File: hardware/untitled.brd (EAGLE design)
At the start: 68.6 x 47.9 mm, 47 parts, among them IC2 LM1117IMPX-3.3, U4 microSD, Y1 CRYSTAL-GROUNDEDSMD-5X3.2

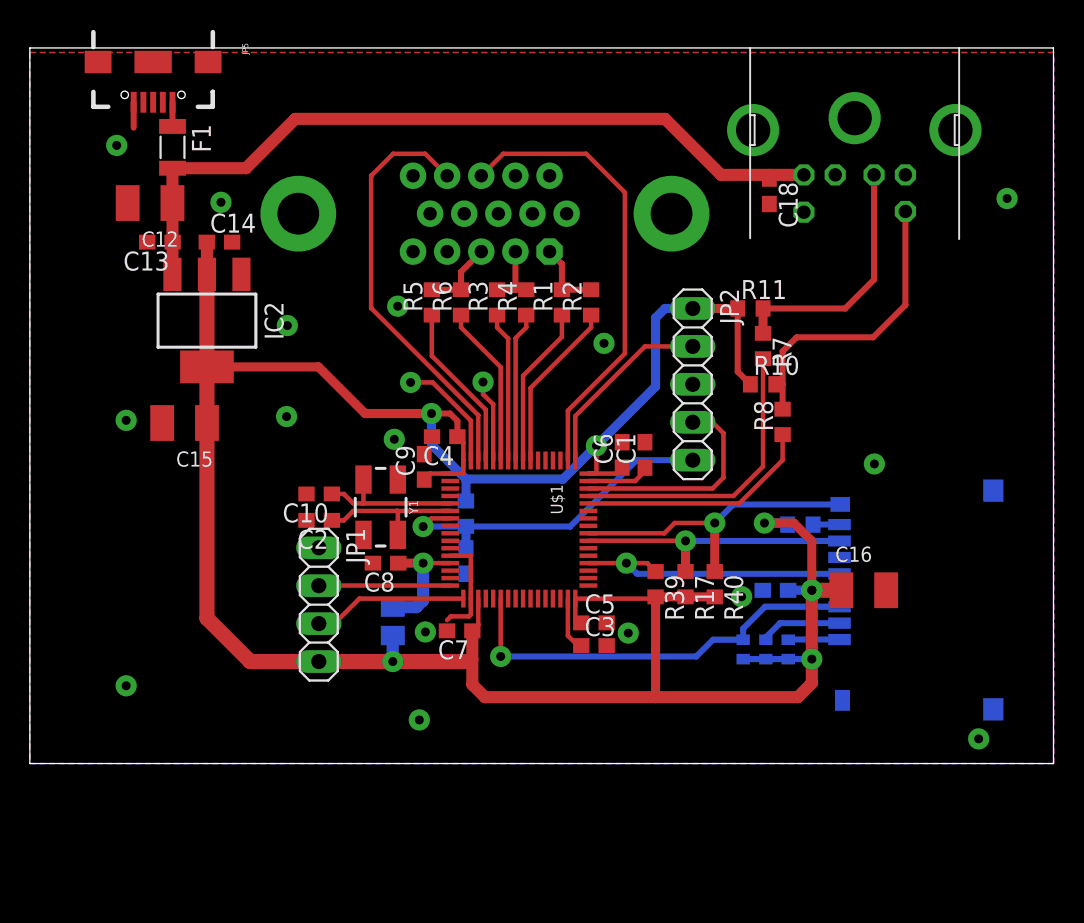
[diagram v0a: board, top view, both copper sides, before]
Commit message: Proper MCU footprint used
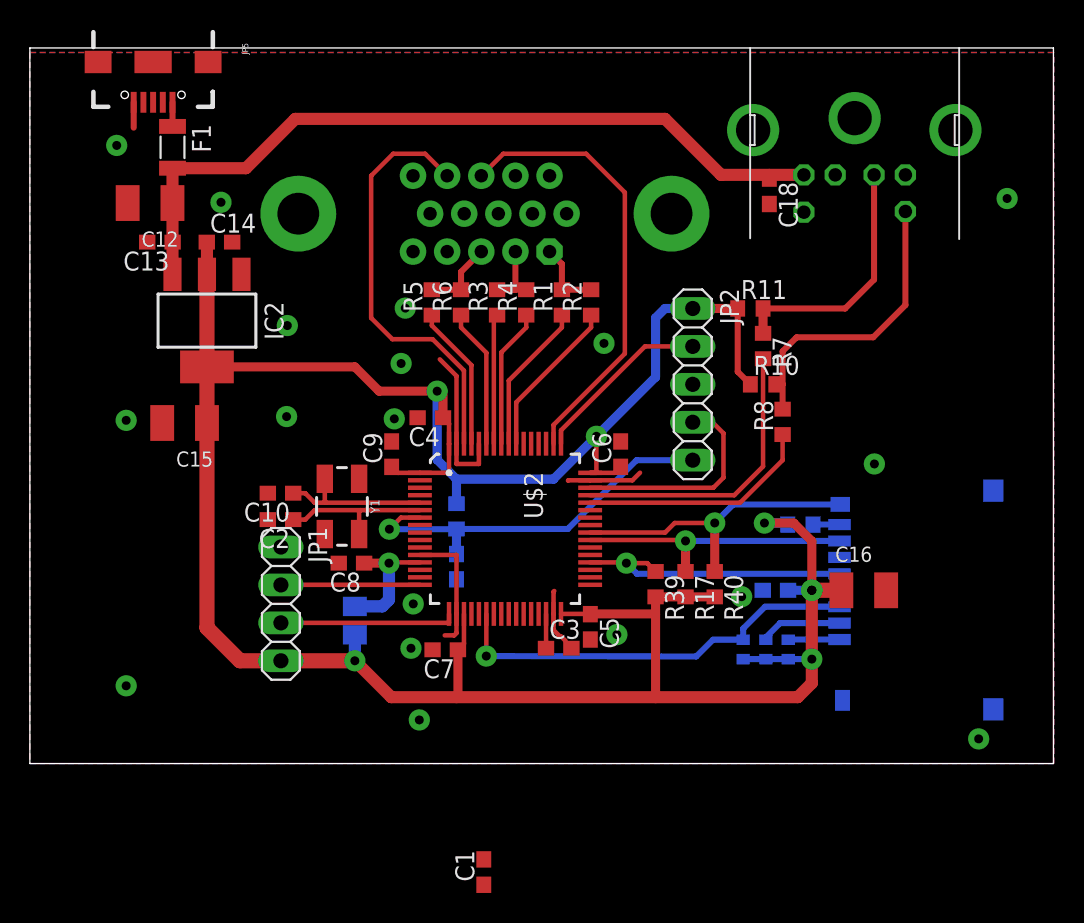
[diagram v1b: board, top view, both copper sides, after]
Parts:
- removed U$1: STM32F4R_64PIN_FOXCAR, stm32f4:LQFP64
- added U$2: STM32F411XC, stm32f411:LQFP64
- moved C1 30.0 mm to (30.4, -7.27)
- moved Y1 2.59 mm to (20.9, 17.2)
- moved C10 2.59 mm to (16.8, 18.1)
- moved C2 2.59 mm to (16.8, 16.3)
- moved JP1 2.54 mm to (16.8, 10.7)
- moved R9 2.54 mm to (21.8, 9.58)
- moved C3 2.37 mm to (35.4, 7.72)
- moved C9 2.34 mm to (24.2, 20.7)
- moved C8 2.29 mm to (21.5, 13.4)
- moved C4 1.60 mm to (26.8, 23.2)
- moved C7 1.60 mm to (27.8, 7.62)
- moved C17 0.74 mm to (28.6, 13.2)
- moved R12 0.66 mm to (28.6, 16.6)
- moved C5 0.36 mm to (37.5, 9.16), turned to 270 degrees
- moved C6 0.11 mm to (39.6, 20.7)
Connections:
- net 3V: now also U$2.1, U$2.19, U$2.32, U$2.48, U$2.64; no longer U$1.1, U$1.19, U$1.32, U$1.48, U$1.64
- net BLUE0: now also U$2.59; no longer U$1.59
- net BLUE1: now also U$2.61; no longer U$1.61
- net GND: now also U$2.12, U$2.18, U$2.31, U$2.47, U$2.60, U$2.63; no longer U$1.12, U$1.18, U$1.60, U$1.63
- net GREEN0: now also U$2.57; no longer U$1.57
- net GREEN1: now also U$2.58; no longer U$1.58
- net HSYNC: now also U$2.50; no longer U$1.50
- net N$6: now also U$2.13; no longer U$1.13
- net N$7: no longer U$1.47
- net N$8: now also U$2.30; no longer U$1.31
- net NRST: now also U$2.7; no longer U$1.7
- net OSC_IN: now also U$2.5; no longer U$1.5
- net OSC_OUT: now also U$2.6; no longer U$1.6
- net PS2_CLK: now also U$2.44; no longer U$1.44
- net PS2_DAT: now also U$2.45; no longer U$1.45
- net RED0: now also U$2.55; no longer U$1.55
- net RED1: now also U$2.56; no longer U$1.56
- net SDIO_CD: now also U$2.40; no longer U$1.40
- net SDIO_CLK: now also U$2.36; no longer U$1.36
- net SDIO_CMD: now also U$2.22; no longer U$1.22
- net SDIO_D0: now also U$2.39; no longer U$1.39
- net SWD_CLK: now also U$2.49; no longer U$1.49
- net SWD_IO: now also U$2.46; no longer U$1.46
- net UART2_RX: now also U$2.17; no longer U$1.17
- net UART2_TX: now also U$2.16; no longer U$1.16
- net VSYNC: now also U$2.62; no longer U$1.62
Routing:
- net GND: track 22.1 -> 29.4 mm
- net N$7: track 4.30 -> 0.00 mm
- net 3V: track 185.5 -> 188.9 mm
- net NRST: track 23.4 -> 26.3 mm
- net BLUE1: track 11.2 -> 9.71 mm
- net BLUE0: track 10.8 -> 9.32 mm
- net UART2_RX: track 10.4 -> 11.9 mm
- net N$8: track 3.66 -> 2.30 mm
- net GREEN1: track 10.0 -> 8.70 mm
- net N$6: track 8.20 -> 9.07 mm
- net RED0: track 11.4 -> 10.7 mm
- net SWD_CLK: track 12.8 -> 12.0 mm
- net RED1: track 10.8 -> 10.1 mm
- net HSYNC: track 30.8 -> 30.1 mm
- net GREEN0: track 10.0 -> 9.31 mm
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
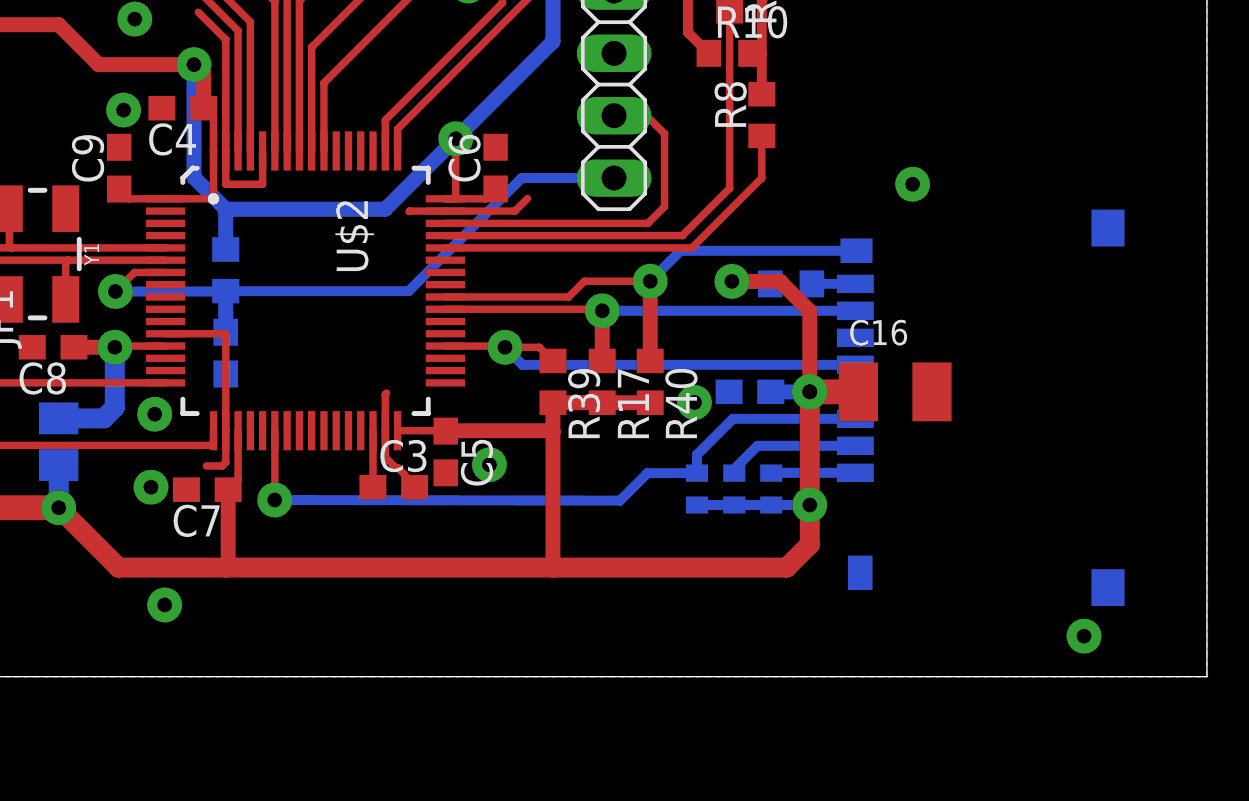
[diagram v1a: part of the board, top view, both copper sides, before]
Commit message: Capacitor removed
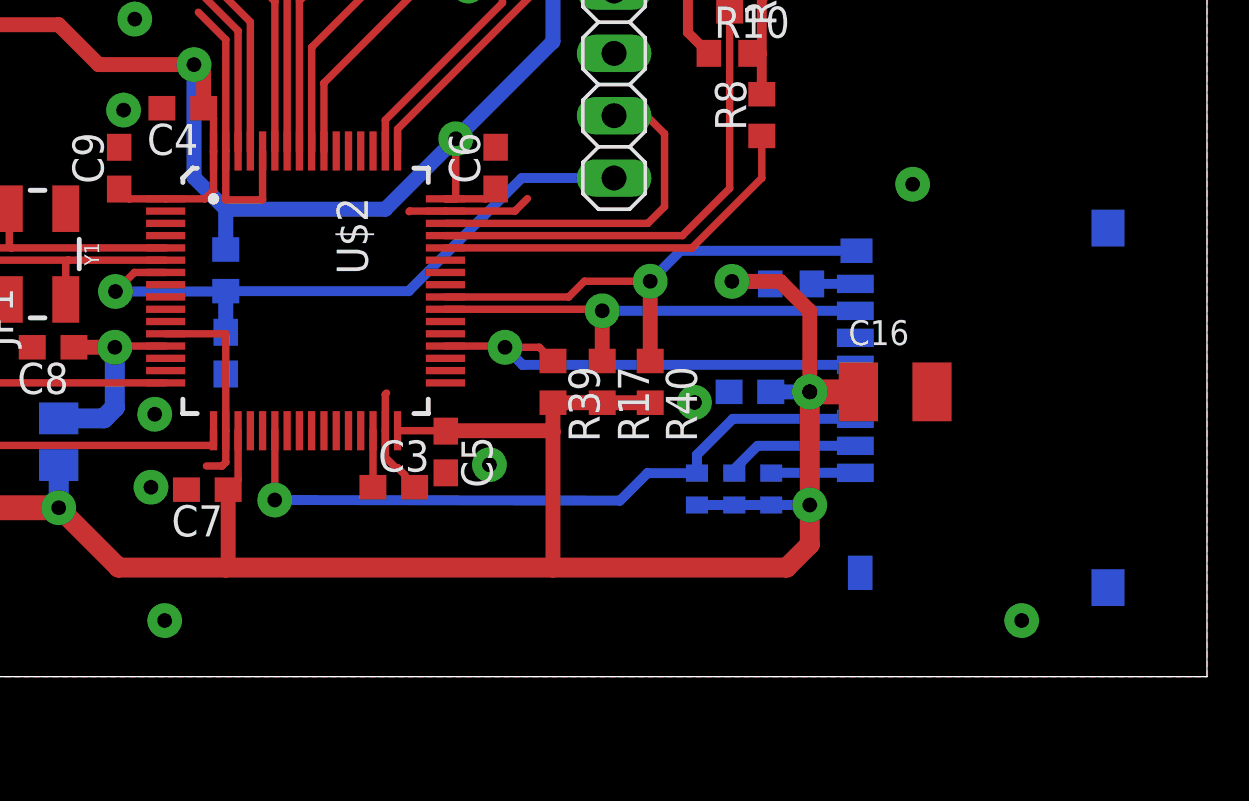
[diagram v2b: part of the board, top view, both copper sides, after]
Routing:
- net GND: track 29.4 -> 30.6 mm
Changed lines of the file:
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@@
 <via x="6.4516" y="5.207" extent="1-16" drill="0.6" diameter="1.4224" shape="octagon"/>
 <via x="65.4558" y="37.846" extent="1-16" drill="0.6" diameter="1.4224" shape="octagon"/>
-<via x="63.5508" y="1.651" extent="1-16" drill="0.6" diameter="1.4224" shape="octagon"/>
+<via x="61.0108" y="2.286" extent="1-16" drill="0.6" diameter="1.4224" shape="octagon"/>
 <via x="17.1958" y="23.241" extent="1-16" drill="0.6" diameter="1.4224" shape="octagon"/>
-<via x="26.0858" y="2.921" extent="1-16" drill="0.6" diameter="1.4224" shape="octagon"/>
+<via x="26.0858" y="2.286" extent="1-16" drill="0.6" diameter="1.4224" shape="octagon"/>
 <contactref element="C18" pad="2"/>
 <contactref element="U$2" pad="12"/>
@@
 <wire x1="28.5762" y1="21.4226" x2="28.5762" y2="25.9576" width="0.3048" layer="1"/>
 <wire x1="28.5762" y1="25.9576" x2="27.4574" y2="27.0764" width="0.3048" layer="1"/>
-<wire x1="28.5762" y1="21.4226" x2="28.5762" y2="20.066" width="0.3048" layer="1"/>
-<wire x1="28.5762" y1="20.066" x2="30.0762" y2="20.066" width="0.3048" layer="1"/>
-<wire x1="30.0762" y1="20.066" x2="30.0762" y2="21.4226" width="0.3048" layer="1"/>
+<wire x1="28.5762" y1="21.4226" x2="28.5762" y2="19.431" width="0.3048" layer="1"/>
+<wire x1="28.5762" y1="19.431" x2="30.0762" y2="19.431" width="0.3048" layer="1"/>
+<wire x1="30.0762" y1="19.431" x2="30.0762" y2="21.4226" width="0.3048" layer="1"/>
 <via x="24.8666" y="26.797" extent="1-16" drill="0.6" diameter="1.4224" shape="octagon"/>
 <wire x1="28.5762" y1="10.0226" x2="28.5762" y2="8.7388" width="0.3048" layer="1"/>
@@
 <wire x1="37.5262" y1="18.9726" x2="40.3594" y2="18.9726" width="0.3048" layer="1"/>
 <wire x1="40.3594" y1="18.9726" x2="40.8686" y2="19.4818" width="0.3048" layer="1"/>
-<wire x1="26.0858" y1="2.921" x2="30.4038" y2="-6.41948125" width="0" layer="19" extent="1-1"/>
+<wire x1="26.0858" y1="2.286" x2="30.4038" y2="-6.41948125" width="0" layer="19" extent="1-1"/>
 </signal>
 <signal name="PE1">
@@
 <wire x1="28.0762" y1="21.4226" x2="28.0762" y2="22.761" width="0.3048" layer="1"/>
 <wire x1="28.0762" y1="22.761" x2="27.6724" y2="23.1648" width="0.3048" layer="1"/>
-<wire x1="26.1262" y1="19.4726" x2="28.0762" y2="19.4726" width="0.3048" layer="1"/>
-<wire x1="28.0762" y1="19.4726" x2="28.0762" y2="21.4226" width="0.3048" layer="1"/>
 <wire x1="27.6724" y1="23.1648" x2="27.6724" y2="24.9428" width="0.6096" layer="1"/>
 <wire x1="27.2796" y1="24.9428" x2="23.3934" y2="24.9428" width="0.6096" layer="1"/>
@@
 <wire x1="37.9476" y1="21.9202" x2="37.9476" y2="19.4726" width="0.3048" layer="1"/>
 <wire x1="37.9476" y1="19.4726" x2="37.5262" y2="19.4726" width="0.3048" layer="1"/>
+<wire x1="26.1262" y1="19.4726" x2="27.7276" y2="19.4726" width="0.3048" layer="1"/>
+<wire x1="27.7276" y1="19.4726" x2="28.0762" y2="19.8212" width="0.3048" layer="1"/>
+<wire x1="28.0762" y1="21.4226" x2="28.0762" y2="19.8212" width="0.3048" layer="1"/>
 </signal>
 <signal name="5V">

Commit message: Minor adjustment
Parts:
- removed C1: (no value), rcl:C0603
- moved C12 1.65 mm to (8.05, 35.9)
- moved C15 1.65 mm to (10.4, 21.2)
- moved IC2 1.65 mm to (11.9, 28.0)
- moved C13 1.65 mm to (8.71, 33.3)
- moved C14 1.65 mm to (12.7, 33.3)
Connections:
- removed net N$7: C1.1
- net GND: no longer C1.2
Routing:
- net 3V: track 188.7 -> 186.4 mm
- net 5V: track 52.7 -> 54.3 mm
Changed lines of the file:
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@@
 <attribute name="OC_FARNELL" value="1596988" x="31.78" y="49.53" size="1.778" layer="27" rot="R270" display="off"/>
 </element>
-<element name="C12" library="rcl" package="SMC_B" value="" x="8.0518" y="37.5412" rot="R180"/>
-<element name="C13" library="rcl" package="C0603" value="" x="8.7122" y="34.925" rot="R180"/>
-<element name="C14" library="rcl" package="C0603" value="" x="12.7" y="34.925"/>
-<element name="C15" library="rcl" package="SMC_B" value="" x="10.3632" y="22.8092" rot="R180"/>
-<element name="IC2" library="lm1117" package="SOT223" value="LM1117IMPX-3.3" x="11.8618" y="29.6672" rot="R180"/>
+<element name="C12" library="rcl" package="SMC_B" value="" x="8.0518" y="35.8902" rot="R180"/>
+<element name="C13" library="rcl" package="C0603" value="" x="8.7122" y="33.274" rot="R180"/>
+<element name="C14" library="rcl" package="C0603" value="" x="12.7" y="33.274"/>
+<element name="C15" library="rcl" package="SMC_B" value="" x="10.3632" y="21.1582" rot="R180"/>
+<element name="IC2" library="lm1117" package="SOT223" value="LM1117IMPX-3.3" x="11.8618" y="28.0162" rot="R180"/>
 <element name="JP2" library="pinhead" package="1X05" value="" x="44.3992" y="25.4" rot="R270"/>
 <element name="JP1" library="pinhead" package="1X04" value="" x="16.8148" y="10.6934" rot="R270"/>
@@
 <element name="C10" library="rcl" package="C0603" value="22 pF" x="16.7894" y="18.1084" rot="R180"/>
 <element name="Y1" library="SparkFun-Clocks" package="CRYSTAL-SMD-5X3.2-4PAD" value="CRYSTAL-GROUNDEDSMD-5X3.2" x="20.9042" y="17.2212" rot="R270"/>
-<element name="C1" library="rcl" package="C0603" value="" x="30.4038" y="-7.26948125" rot="R90"/>
 <element name="C3" library="rcl" package="C0603" value="" x="35.42156875" y="7.7216"/>
 <element name="U4" library="SparkFun-Connectors" package="USD-SOCKET-PP" value="microSD" x="68.5292" y="11.5062" rot="MR270"/>
@@
 <contactref element="Y1" pad="4"/>
 <contactref element="Y1" pad="2"/>
-<contactref element="C1" pad="2"/>
 <contactref element="C3" pad="2"/>
 <contactref element="U4" pad="6"/>
@@
 <via x="25.146" y="30.5054" extent="1-16" drill="0.6" diameter="1.4224" shape="octagon"/>
 <contactref element="C9" pad="2"/>
-<via x="12.8016" y="37.592" extent="1-16" drill="0.6" diameter="1.4224" shape="octagon"/>
+<via x="12.8016" y="35.941" extent="1-16" drill="0.6" diameter="1.4224" shape="octagon"/>
 <via x="17.2466" y="29.337" extent="1-16" drill="0.6" diameter="1.4224" shape="octagon"/>
-<via x="6.4516" y="22.987" extent="1-16" drill="0.6" diameter="1.4224" shape="octagon"/>
+<via x="6.4516" y="21.336" extent="1-16" drill="0.6" diameter="1.4224" shape="octagon"/>
 <via x="5.8166" y="41.402" extent="1-16" drill="0.6" diameter="1.4224" shape="octagon"/>
 <contactref element="C11" pad="2"/>
@@
 <wire x1="37.5262" y1="18.9726" x2="40.3594" y2="18.9726" width="0.3048" layer="1"/>
 <wire x1="40.3594" y1="18.9726" x2="40.8686" y2="19.4818" width="0.3048" layer="1"/>
-<wire x1="26.0858" y1="2.286" x2="30.4038" y2="-6.41948125" width="0" layer="19" extent="1-1"/>
 </signal>
 <signal name="PE1">
@@
 <contactref element="IC2" pad="TAB"/>
 <contactref element="IC2" pad="2"/>
-<wire x1="11.8618" y1="32.7662" x2="11.8618" y2="34.9132" width="0.8128" layer="1"/>
-<wire x1="11.8618" y1="34.9132" x2="11.85" y2="34.925" width="0.6096" layer="1"/>
+<wire x1="11.8618" y1="31.1152" x2="11.8618" y2="33.2622" width="0.8128" layer="1"/>
+<wire x1="11.8618" y1="33.2622" x2="11.85" y2="33.274" width="0.6096" layer="1"/>
 <contactref element="JP2" pad="1"/>
 <contactref element="JP1" pad="4"/>
@@
 <via x="37.9476" y="21.9202" extent="1-16" drill="0.6" diameter="1.4224" shape="octagon"/>
 <contactref element="C9" pad="1"/>
-<wire x1="11.8618" y1="32.7662" x2="11.8618" y2="26.5682" width="1.016" layer="1"/>
-<wire x1="11.8632" y1="22.8092" x2="11.8632" y2="26.5668" width="1.016" layer="1"/>
-<wire x1="11.8632" y1="26.5668" x2="11.8618" y2="26.5682" width="1.016" layer="1"/>
-<wire x1="11.8618" y1="26.5682" x2="21.768" y2="26.5682" width="0.6096" layer="1"/>
-<wire x1="11.8632" y1="22.8092" x2="11.8632" y2="9.0918" width="1.016" layer="1"/>
+<wire x1="11.8618" y1="31.1152" x2="11.8618" y2="24.9172" width="1.016" layer="1"/>
+<wire x1="11.8632" y1="21.1582" x2="11.8632" y2="24.9158" width="1.016" layer="1"/>
+<wire x1="11.8632" y1="24.9158" x2="11.8618" y2="24.9172" width="1.016" layer="1"/>
+<wire x1="11.8632" y1="21.1582" x2="11.8632" y2="9.0918" width="1.016" layer="1"/>
 <wire x1="35.0774" y1="19.05" x2="28.575" y2="19.05" width="0.6096" layer="16"/>
 <wire x1="44.3992" y1="30.48" x2="42.545" y2="30.48" width="0.6096" layer="16"/>
@@
 <wire x1="28.0762" y1="22.761" x2="27.6724" y2="23.1648" width="0.3048" layer="1"/>
 <wire x1="27.6724" y1="23.1648" x2="27.6724" y2="24.9428" width="0.6096" layer="1"/>
-<wire x1="27.2796" y1="24.9428" x2="23.3934" y2="24.9428" width="0.6096" layer="1"/>
-<wire x1="23.3934" y1="24.9428" x2="21.768" y2="26.5682" width="0.6096" layer="1"/>
+<wire x1="27.2796" y1="24.9428" x2="11.8874" y2="24.9428" width="0.6096" layer="1"/>
 <wire x1="26.1262" y1="19.4726" x2="24.63031875" y2="19.4726" width="0.3048" layer="1"/>
 <wire x1="24.63031875" y1="19.4726" x2="24.2316" y2="19.87131875" width="0.3048" layer="1"/>
@@
 <wire x1="27.7276" y1="19.4726" x2="28.0762" y2="19.8212" width="0.3048" layer="1"/>
 <wire x1="28.0762" y1="21.4226" x2="28.0762" y2="19.8212" width="0.3048" layer="1"/>
+<wire x1="11.8874" y1="24.9428" x2="11.8618" y2="24.9172" width="0.6096" layer="1"/>
 </signal>
 <signal name="5V">
@@
 <contactref element="IC2" pad="3"/>
 <contactref element="F1" pad="2"/>
-<wire x1="9.555" y1="39.875" x2="9.555" y2="37.465" width="0.8128" layer="1"/>
-<wire x1="9.555" y1="37.465" x2="9.555" y2="34.925" width="0.8128" layer="1"/>
-<wire x1="9.555" y1="34.925" x2="9.555" y2="32.7704" width="0.8128" layer="1"/>
-<wire x1="9.555" y1="32.7704" x2="9.5508" y2="32.7662" width="0.8128" layer="1"/>
-<wire x1="9.5622" y1="34.925" x2="9.555" y2="34.925" width="0.4064" layer="1"/>
-<wire x1="9.5518" y1="37.5412" x2="9.5518" y2="37.4682" width="0.4064" layer="1"/>
-<wire x1="9.5518" y1="37.4682" x2="9.555" y2="37.465" width="0.4064" layer="1"/>
+<wire x1="9.555" y1="39.875" x2="9.555" y2="35.814" width="0.8128" layer="1"/>
+<wire x1="9.555" y1="35.814" x2="9.555" y2="33.274" width="0.8128" layer="1"/>
+<wire x1="9.555" y1="33.274" x2="9.555" y2="31.1194" width="0.8128" layer="1"/>
+<wire x1="9.555" y1="31.1194" x2="9.5508" y2="31.1152" width="0.8128" layer="1"/>
+<wire x1="9.5622" y1="33.274" x2="9.555" y2="33.274" width="0.4064" layer="1"/>
+<wire x1="9.5518" y1="35.8902" x2="9.5518" y2="35.8172" width="0.4064" layer="1"/>
+<wire x1="9.5518" y1="35.8172" x2="9.555" y2="35.814" width="0.4064" layer="1"/>
 <wire x1="9.555" y1="39.875" x2="14.475" y2="39.875" width="0.8128" layer="1"/>
 <wire x1="14.475" y1="39.875" x2="17.78" y2="43.18" width="0.8128" layer="1"/>
@@
 <wire x1="19.7542" y1="17.5558" x2="19.8374" y2="17.4726" width="0.3048" layer="1"/>
 </signal>
-<signal name="N$7">
-<contactref element="C1" pad="1"/>
-</signal>
 <signal name="N$8">
